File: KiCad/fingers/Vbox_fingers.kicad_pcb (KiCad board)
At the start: 2 copper layers, 109 x 45 mm, 20 parts, among them J1 Conn_01x10, J2 Conn_01x10, SW1 SW_Push_45deg, SW10 SW_Push_45deg, SW11 SW_Push_45deg, SW12 SW_Push_45deg, SW13 SW_Push_45deg, SW14 SW_Push_45deg, SW15 SW_Push_45deg, SW16 SW_Push_45deg, SW17 SW_Push_45deg, SW18 SW_Push_45deg, SW2 SW_Push_45deg, SW3 SW_Push_45deg, SW4 SW_Push_45deg, SW5 SW_Push_45deg, SW6 SW_Push_45deg, SW7 SW_Push_45deg, SW8 SW_Push_45deg, SW9 SW_Push_45deg

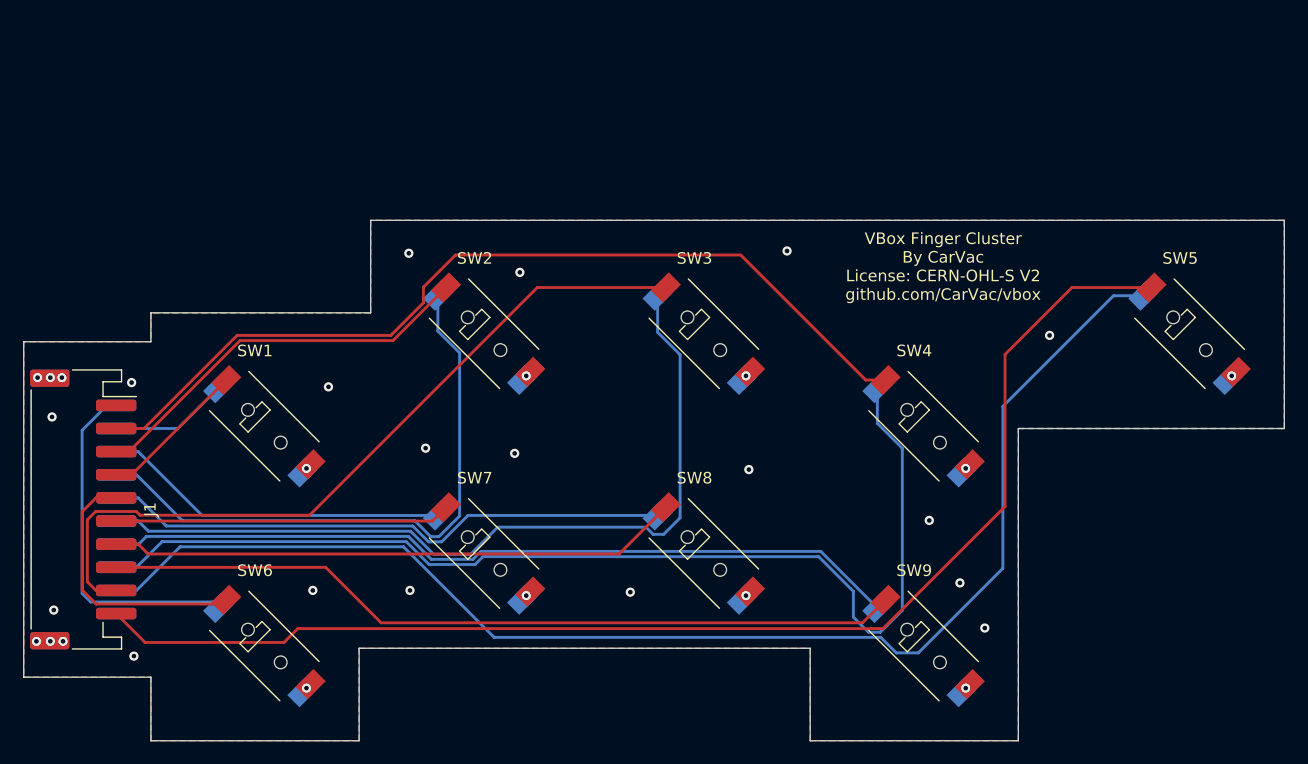
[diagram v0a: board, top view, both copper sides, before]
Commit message: make start button lower
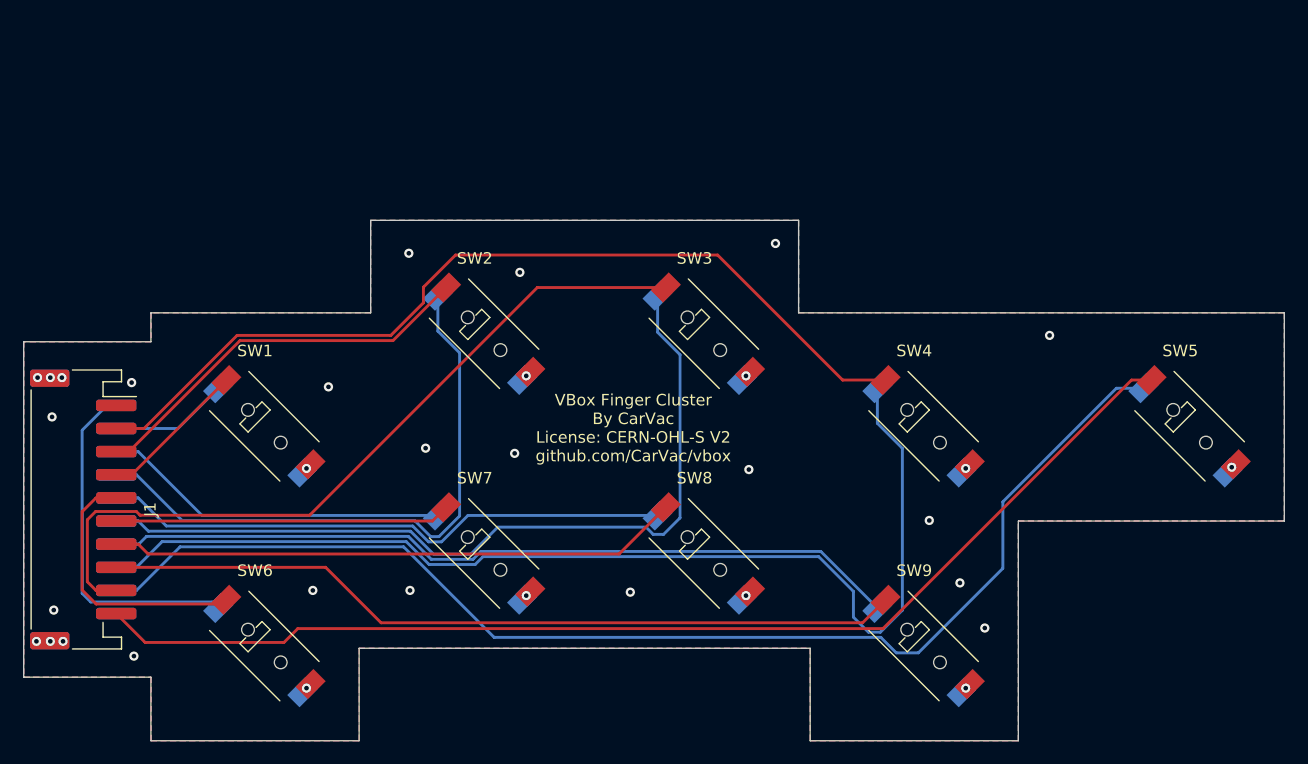
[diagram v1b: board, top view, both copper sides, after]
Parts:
- moved SW14 8.00 mm to (180.0, 100.0)
- moved SW5 8.00 mm to (180.0, 100.0)
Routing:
- net START: track 111.0 -> 100.0 mm
- net RIGHTSTART: track 115.2 -> 107.0 mm
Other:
- outline, holes or cut-outs redrawn
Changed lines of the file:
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@@
   )
   (footprint "Buttons:Vbox" (layer "F.Cu")
-    (at 180 92)
+    (at 180 100)
     (property "Sheetfile" "Vbox_fingers.kicad_sch")
     (property "Sheetname" "")
@@
   )
   (footprint "Buttons:Vbox_1" (layer "B.Cu")
-    (at 180 92 180)
+    (at 180 100 180)
     (property "Sheetfile" "Vbox_fingers.kicad_sch")
     (property "Sheetname" "")
@@
       (xy 148 128)
       (xy 166 128)
-      (xy 166 101)
-      (xy 189 101)
-      (xy 189 83)
+      (xy 166 109)
+      (xy 189 109)
+      (xy 189 91)
+      (xy 147 91)
+      (xy 147 83)
       (xy 110 83)
       (xy 110 91)
@@
     )
     (stroke (width 0.1) (type solid)) (fill none) (layer "Edge.Cuts"))
-  (gr_text "VBox Finger Cluster\nBy CarVac\nLicense: CERN-OHL-S V2\ngithub.com/CarVac/vbox" (at 159.5 90) (layer "F.SilkS")
+  (gr_text "VBox Finger Cluster\nBy CarVac\nLicense: CERN-OHL-S V2\ngithub.com/CarVac/vbox" (at 132.71 103.96) (layer "F.SilkS")
     (effects (font (size 1 1) (thickness 0.15)) (justify bottom))
   )
@@
   (via (at 122.9 87.5) (size 0.8) (drill 0.4) (layers "F.Cu" "B.Cu") (free) (net 1))
   (via (at 114.75 102.7) (size 0.8) (drill 0.4) (layers "F.Cu" "B.Cu") (free) (net 1))
-  (via (at 146 85.65) (size 0.8) (drill 0.4) (layers "F.Cu" "B.Cu") (free) (net 1))
+  (via (at 145 85) (size 0.8) (drill 0.4) (layers "F.Cu" "B.Cu") (free) (net 1))
   (via (at 161.45 104.45) (size 0.8) (drill 0.4) (layers "F.Cu" "B.Cu") (free) (net 1))
   (via (at 104.45 123.45) (size 0.8) (drill 0.4) (layers "F.Cu" "B.Cu") (free) (net 1))
   (via (at 105 115) (size 0.8) (drill 0.4) (layers "F.Cu" "B.Cu") (free) (net 1))
-  (via (at 184.45 96.45) (size 0.8) (drill 0.4) (layers "F.Cu" "B.Cu") (free) (net 1))
+  (via (at 184.45 104.35) (size 0.8) (drill 0.4) (layers "F.Cu" "B.Cu") (free) (net 1))
   (via (at 104.45 104.45) (size 0.8) (drill 0.4) (layers "F.Cu" "B.Cu") (free) (net 1))
   (via (at 82.6 116.7) (size 0.8) (drill 0.4) (layers "F.Cu" "B.Cu") (free) (net 1))
@@
   (via (at 82.3 119.4) (size 0.8) (drill 0.4) (layers "F.Cu" "B.Cu") (net 1))
   (via (at 123.45 96.45) (size 0.8) (drill 0.4) (layers "F.Cu" "B.Cu") (free) (net 1))
-  (segment (start 170.639051 88.810949) (end 164.85 94.6) (width 0.25) (layer "F.Cu") (net 2))
-  (segment (start 164.85 94.6) (end 164.85 107.75) (width 0.25) (layer "F.Cu") (net 2))
-  (segment (start 90.5 119.5) (end 88 117) (width 0.25) (layer "F.Cu") (net 2))
-  (segment (start 102.5 119.5) (end 90.5 119.5) (width 0.25) (layer "F.Cu") (net 2))
-  (segment (start 154.3 118.3) (end 103.7 118.3) (width 0.25) (layer "F.Cu") (net 2))
-  (segment (start 103.7 118.3) (end 102.5 119.5) (width 0.25) (layer "F.Cu") (net 2))
-  (segment (start 177.518056 88.810949) (end 170.639051 88.810949) (width 0.25) (layer "F.Cu") (net 2))
-  (segment (start 164.85 107.75) (end 154.3 118.3) (width 0.25) (layer "F.Cu") (net 2))
+  (segment (start 88 117) (end 90.5 119.5) (width 0.25) (layer "F.Cu") (net 2))
+  (segment (start 103.7 118.3) (end 154.3 118.3) (width 0.25) (layer "F.Cu") (net 2))
+  (segment (start 90.5 119.5) (end 102.5 119.5) (width 0.25) (layer "F.Cu") (net 2))
+  (segment (start 175.789051 96.810949) (end 177.518056 96.810949) (width 0.25) (layer "F.Cu") (net 2))
+  (segment (start 154.3 118.3) (end 175.789051 96.810949) (width 0.25) (layer "F.Cu") (net 2))
+  (segment (start 102.5 119.5) (end 103.7 118.3) (width 0.25) (layer "F.Cu") (net 2))
   (segment (start 88 113) (end 106.1 113) (width 0.25) (layer "F.Cu") (net 3))
   (segment (start 106.1 113) (end 110.9 117.8) (width 0.25) (layer "F.Cu") (net 3))
@@
   (segment (start 88 103) (end 89.1 103) (width 0.25) (layer "F.Cu") (net 9))
   (segment (start 90.4 101) (end 98.45 92.95) (width 0.25) (layer "F.Cu") (net 10))
+  (segment (start 150.810949 96.810949) (end 154.518056 96.810949) (width 0.25) (layer "F.Cu") (net 10))
+  (segment (start 140 86) (end 150.810949 96.810949) (width 0.25) (layer "F.Cu") (net 10))
+  (segment (start 111.742609 92.95) (end 114.56 90.132609) (width 0.25) (layer "F.Cu") (net 10))
+  (segment (start 117.34 86) (end 140 86) (width 0.25) (layer "F.Cu") (net 10))
+  (segment (start 114.56 88.78) (end 117.34 86) (width 0.25) (layer "F.Cu") (net 10))
+  (segment (start 88 101) (end 90.4 101) (width 0.25) (layer "F.Cu") (net 10))
   (segment (start 114.56 90.132609) (end 114.56 88.78) (width 0.25) (layer "F.Cu") (net 10))
-  (segment (start 152.810949 96.810949) (end 154.518056 96.810949) (width 0.25) (layer "F.Cu") (net 10))
-  (segment (start 88 101) (end 90.4 101) (width 0.25) (layer "F.Cu") (net 10))
-  (segment (start 117.34 86) (end 142 86) (width 0.25) (layer "F.Cu") (net 10))
-  (segment (start 114.56 88.78) (end 117.34 86) (width 0.25) (layer "F.Cu") (net 10))
-  (segment (start 142 86) (end 152.810949 96.810949) (width 0.25) (layer "F.Cu") (net 10))
-  (segment (start 111.742609 92.95) (end 114.56 90.132609) (width 0.25) (layer "F.Cu") (net 10))
   (segment (start 98.45 92.95) (end 111.742609 92.95) (width 0.25) (layer "F.Cu") (net 10))
   (segment (start 96.292893 116) (end 85.8 116) (width 0.25) (layer "B.Cu") (net 11))
@@
   (segment (start 135.328796 110.151204) (end 134.428841 110.151204) (width 0.25) (layer "B.Cu") (net 16))
   (segment (start 134.810949 89.518056) (end 134.810949 92.680949) (width 0.25) (layer "B.Cu") (net 16))
-  (segment (start 174.231944 89.518056) (end 176.810949 89.518056) (width 0.25) (layer "B.Cu") (net 17))
   (segment (start 157.35 120.4) (end 164.66 113.09) (width 0.25) (layer "B.Cu") (net 17))
   (segment (start 154.11 119.06) (end 155.45 120.4) (width 0.25) (layer "B.Cu") (net 17))
-  (segment (start 89.75 115) (end 88 115) (width 0.25) (layer "B.Cu") (net 17))
-  (segment (start 93.52 111.23) (end 89.75 115) (width 0.25) (layer "B.Cu") (net 17))
-  (segment (start 164.66 99.09) (end 174.231944 89.518056) (width 0.25) (layer "B.Cu") (net 17))
-  (segment (start 164.66 113.09) (end 164.66 99.09) (width 0.25) (layer "B.Cu") (net 17))
+  (segment (start 89.75 115) (end 93.52 111.23) (width 0.25) (layer "B.Cu") (net 17))
+  (segment (start 164.66 113.09) (end 164.66 107.34) (width 0.25) (layer "B.Cu") (net 17))
+  (segment (start 164.66 107.34) (end 174.481944 97.518056) (width 0.25) (layer "B.Cu") (net 17))
   (segment (start 120.68 119.06) (end 154.11 119.06) (width 0.25) (layer "B.Cu") (net 17))
-  (segment (start 112.85 111.23) (end 93.52 111.23) (width 0.25) (layer "B.Cu") (net 17))
+  (segment (start 88 115) (end 89.75 115) (width 0.25) (layer "B.Cu") (net 17))
   (segment (start 112.85 111.23) (end 120.68 119.06) (width 0.25) (layer "B.Cu") (net 17))
   (segment (start 155.45 120.4) (end 157.35 120.4) (width 0.25) (layer "B.Cu") (net 17))
+  (segment (start 174.481944 97.518056) (end 176.810949 97.518056) (width 0.25) (layer "B.Cu") (net 17))
+  (segment (start 93.52 111.23) (end 112.85 111.23) (width 0.25) (layer "B.Cu") (net 17))
   (segment (start 119.526396 111.63) (end 118.846396 112.31) (width 0.25) (layer "B.Cu") (net 18))
   (segment (start 148.922893 111.63) (end 119.526396 111.63) (width 0.25) (layer "B.Cu") (net 18))
@@
         (xy 148 128)
         (xy 166 128)
-        (xy 166 101)
-        (xy 189 101)
-        (xy 189 83)
+        (xy 166 109)
+        (xy 189 109)
+        (xy 189 91)
+        (xy 147 91)
+        (xy 147 83)
         (xy 110 83)
         (xy 110 91)
@@
         (xy 148 128)
         (xy 166 128)
-        (xy 166 101)
-        (xy 189 101)
-        (xy 189 83)
+        (xy 166 109)
+        (xy 189 109)
+        (xy 189 91)
+        (xy 147 91)
+        (xy 147 83)
         (xy 110 83)
         (xy 110 91)

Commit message: adjust finger ergo, pullup resistors on mobo
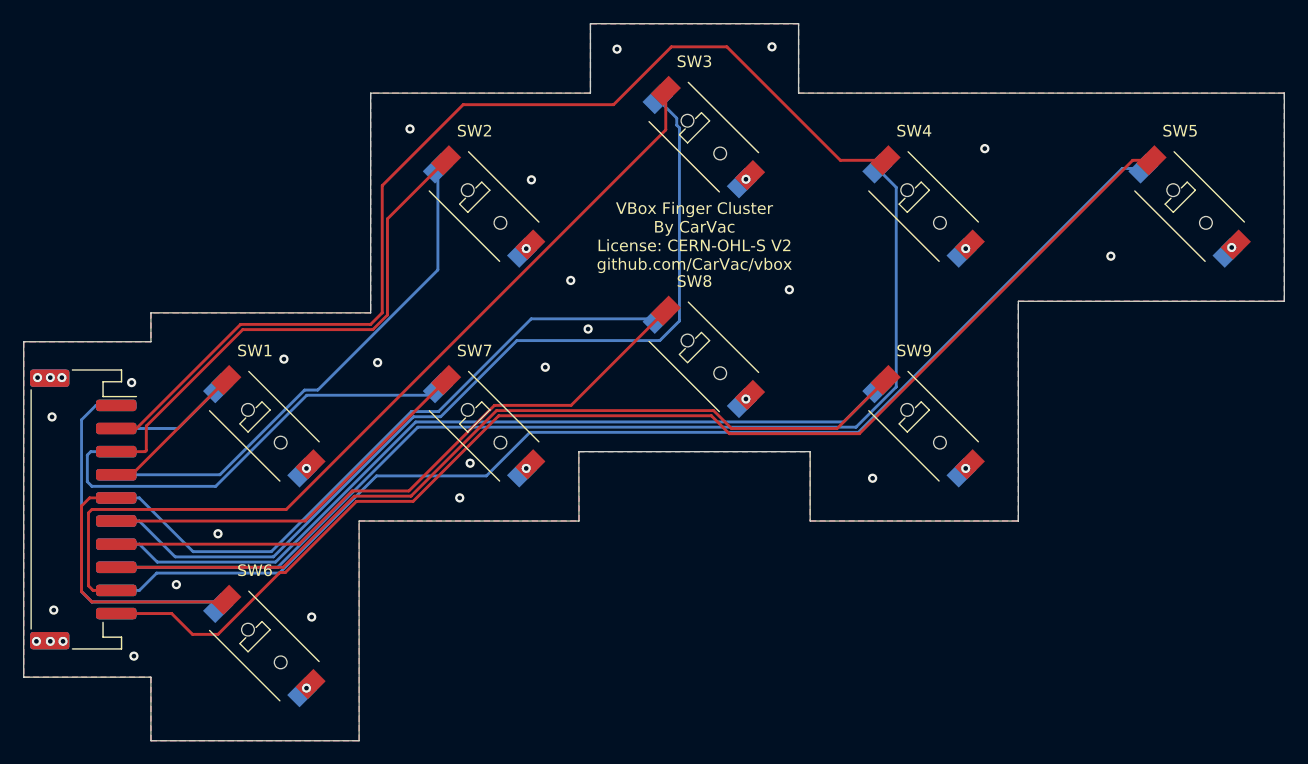
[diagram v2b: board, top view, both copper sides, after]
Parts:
- moved SW13 19.0 mm to (157.0, 81.0)
- moved SW14 19.0 mm to (180.0, 81.0)
- moved SW18 19.0 mm to (157.0, 100.0)
- moved SW4 19.0 mm to (157.0, 81.0)
- moved SW5 19.0 mm to (180.0, 81.0)
- moved SW9 19.0 mm to (157.0, 100.0)
- moved SW12 17.0 mm to (138.0, 75.0)
- moved SW17 17.0 mm to (138.0, 94.0)
- moved SW3 17.0 mm to (138.0, 75.0)
- moved SW8 17.0 mm to (138.0, 94.0)
- moved SW11 11.0 mm to (119.0, 81.0)
- moved SW16 11.0 mm to (119.0, 100.0)
- moved SW2 11.0 mm to (119.0, 81.0)
- moved SW7 11.0 mm to (119.0, 100.0)
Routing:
- net INDEX2: track 78.0 -> 90.7 mm
- net RING2: track 34.4 -> 45.1 mm
- net UP2: track 66.8 -> 75.9 mm
- net START: track 100.0 -> 109.1 mm
- net Z: track 30.1 -> 38.9 mm
- net LS: track 52.5 -> 43.9 mm
- net X: track 49.3 -> 57.1 mm
- net Y: track 71.8 -> 78.4 mm
- net DOWN: track 49.5 -> 55.9 mm
- net RIGHT: track 69.3 -> 74.5 mm
- net LEFT: track 29.0 -> 33.6 mm
- net B: track 69.2 -> 72.7 mm
- net RIGHTSTART: track 107.0 -> 103.9 mm
- net R: track 94.9 -> 93.5 mm
- net L: track 23.3 -> 24.2 mm
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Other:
- board size 109 x 45 mm -> 109 x 62 mm

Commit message: flatten finger clusters slightly
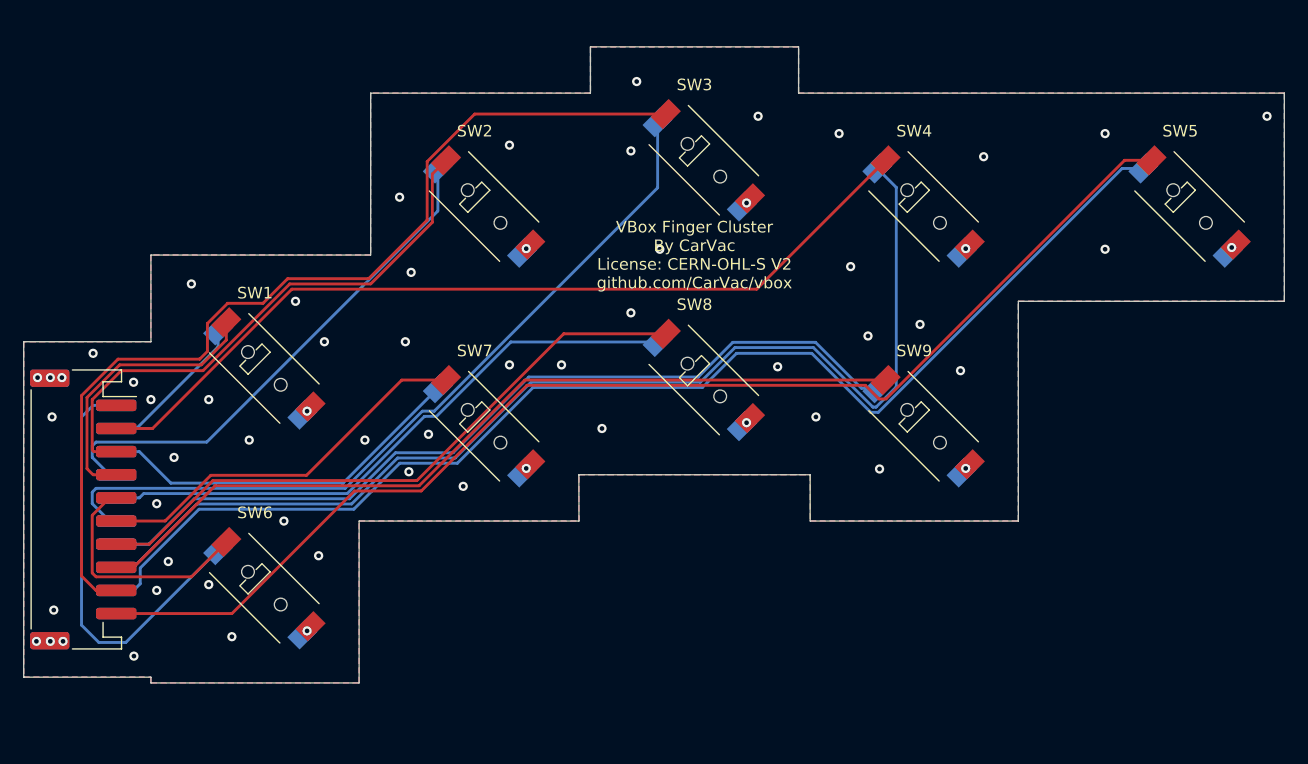
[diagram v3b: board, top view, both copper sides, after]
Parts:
- moved SW1 5.00 mm to (100.0, 95.0)
- moved SW10 5.00 mm to (100.0, 95.0)
- moved SW15 5.00 mm to (100.0, 114.0)
- moved SW6 5.00 mm to (100.0, 114.0)
- moved SW12 2.00 mm to (138.0, 77.0)
- moved SW17 2.00 mm to (138.0, 96.0)
- moved SW3 2.00 mm to (138.0, 77.0)
- moved SW8 2.00 mm to (138.0, 96.0)
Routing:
- net INDEX2: track 90.7 -> 76.1 mm
- net PINKY2: track 12.9 -> 24.5 mm
- net Y: track 78.4 -> 69.1 mm
- net UP2: track 75.9 -> 84.1 mm
- net Z: track 38.9 -> 32.3 mm
- net UP: track 30.8 -> 37.2 mm
- net RIGHTSTART: track 103.9 -> 108.9 mm
- net X: track 57.1 -> 52.4 mm
- net R: track 93.5 -> 97.7 mm
- net L: track 24.2 -> 20.7 mm
- net RING2: track 45.1 -> 48.1 mm
- net MS: track 10.3 -> 13.2 mm
- net B: track 72.7 -> 74.7 mm
- net START: track 109.1 -> 107.3 mm
- net LS: track 43.9 -> 45.7 mm
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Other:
- board size 109 x 62 mm -> 109 x 55 mm
